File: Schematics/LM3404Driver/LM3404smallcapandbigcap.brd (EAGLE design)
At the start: 103.8 x 106.7 mm, 63 parts, among them IC1 LM3404, IC2 LM3404, IC3 LM3404, IC4 LM3404, IC5 LM3404, IC6 LM3404, J1 POWER_JACKPTH

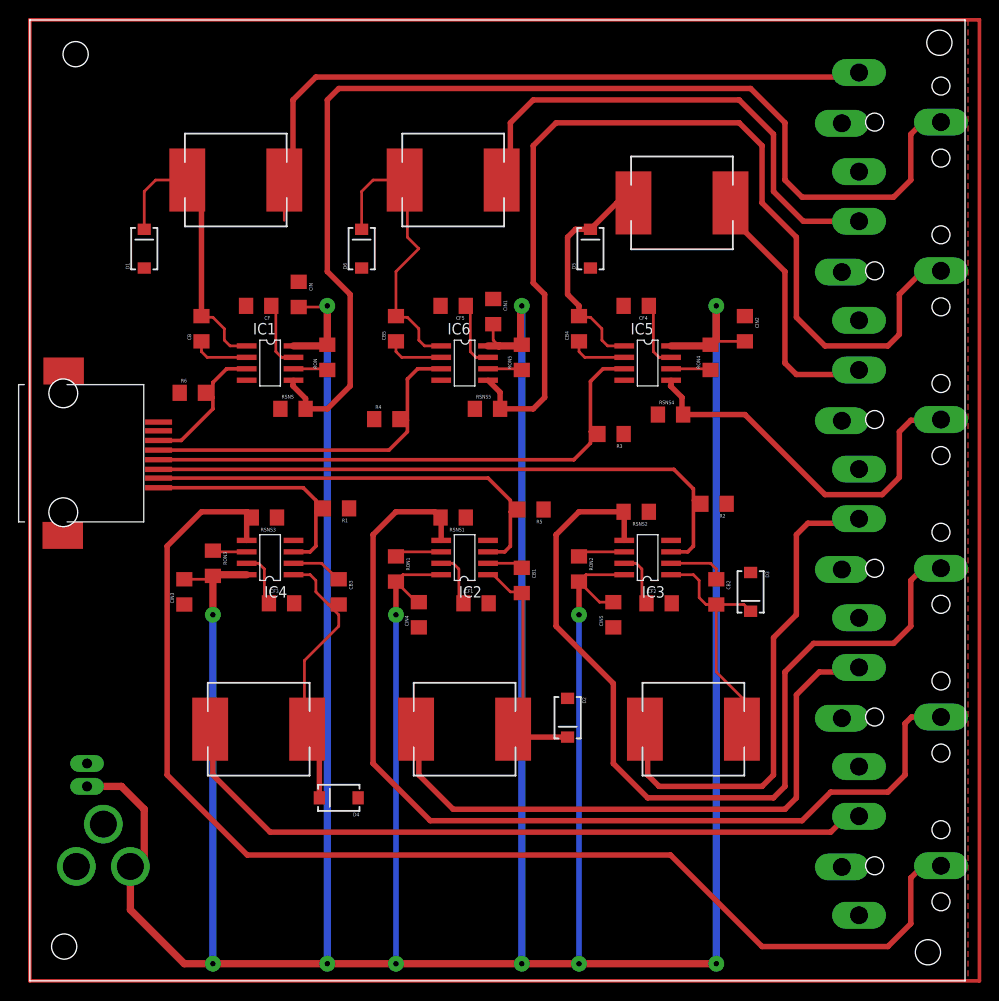
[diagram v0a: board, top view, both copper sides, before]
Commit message: Moving to angular and adding PCA9685 reset to firmware
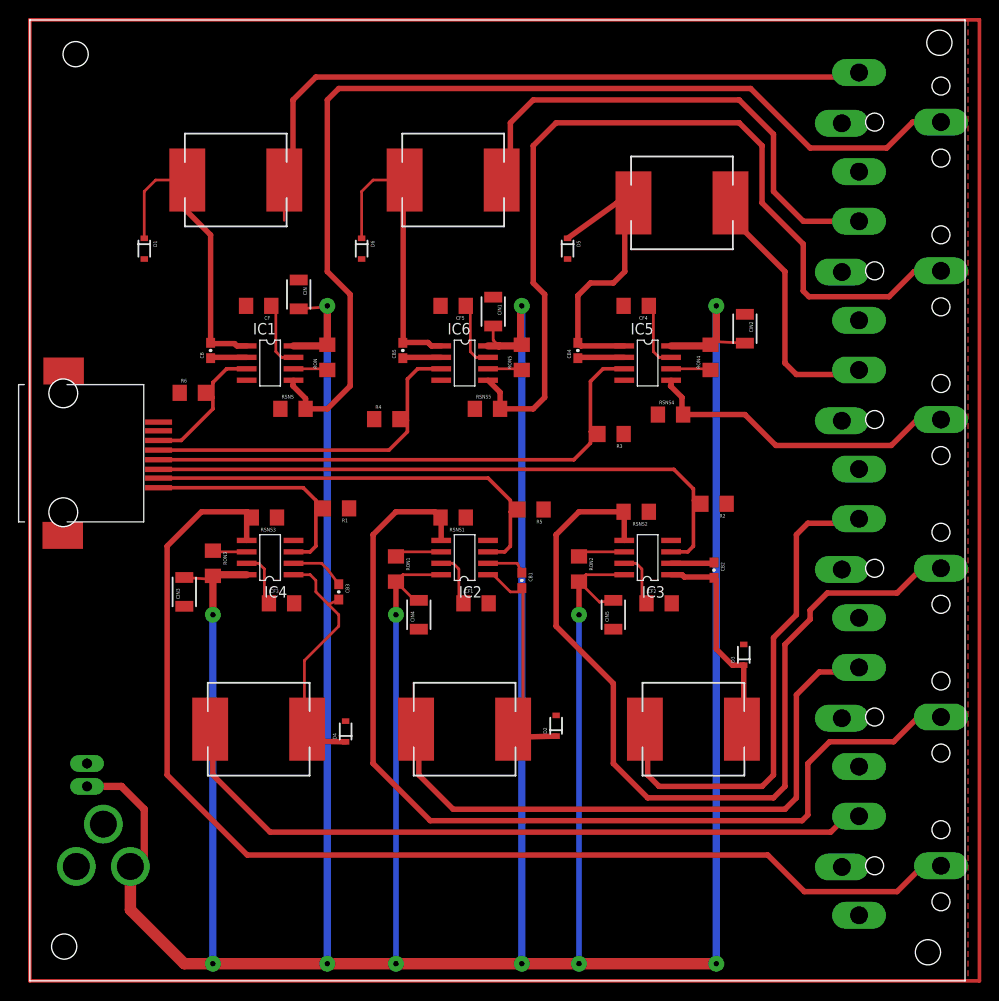
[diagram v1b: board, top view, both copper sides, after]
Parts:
- CB, CB1, CB2, CB3, CB4, CB5: device SparkFun-Capacitors:1206 -> SparkFun-Capacitors:0603-CAP
- CIN, CIN1, CIN2, CIN3, CIN4, CIN5: device SparkFun-Capacitors:1206 -> SparkFun-Capacitors:1210
- D1, D2, D3, D4, D5, D6: value B340A -> PMEG4005EJ; device SparkFun-DiscreteSemi:SMA-DIODE -> SparkFun-DiscreteSemi:SOD-323
- moved D4 7.41 mm to (35.1, 27.7), turned to 90 degrees
- moved D3 7.03 mm to (79.2, 36.2), turned to 90 degrees
- moved CB 2.62 mm to (20.1, 70.0)
- moved D5 2.54 mm to (59.7, 81.3), turned to 270 degrees
- moved CB5 2.53 mm to (41.4, 70.0)
- moved CB2 2.43 mm to (75.9, 45.6)
- moved CB4 2.42 mm to (60.8, 70.0)
- moved D2 1.55 mm to (58.4, 28.3), turned to 90 degrees
- turned D1 to 270 degrees
- turned D6 to 270 degrees
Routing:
- net N$5: track 126.4 -> 115.2 mm
- net N$41: track 109.2 -> 99.9 mm
- net N$27: track 142.3 -> 134.3 mm
- net N$32: track 28.6 -> 36.6 mm
- net N$34: track 43.1 -> 35.8 mm
- net N$4: track 32.4 -> 36.8 mm
- net N$18: track 27.4 -> 23.9 mm
- net N$25: track 31.2 -> 28.0 mm
- net N$2: track 6.42 -> 4.09 mm
- net N$38: track 6.42 -> 4.29 mm
- net N$17: track 6.42 -> 4.80 mm
- net N$31: track 6.42 -> 5.18 mm
- net N$10: track 4.09 -> 4.83 mm
- net N$20: track 98.7 -> 98.1 mm
- net N$11: track 29.3 -> 28.8 mm
